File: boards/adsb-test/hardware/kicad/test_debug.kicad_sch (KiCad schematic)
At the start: 0 parts

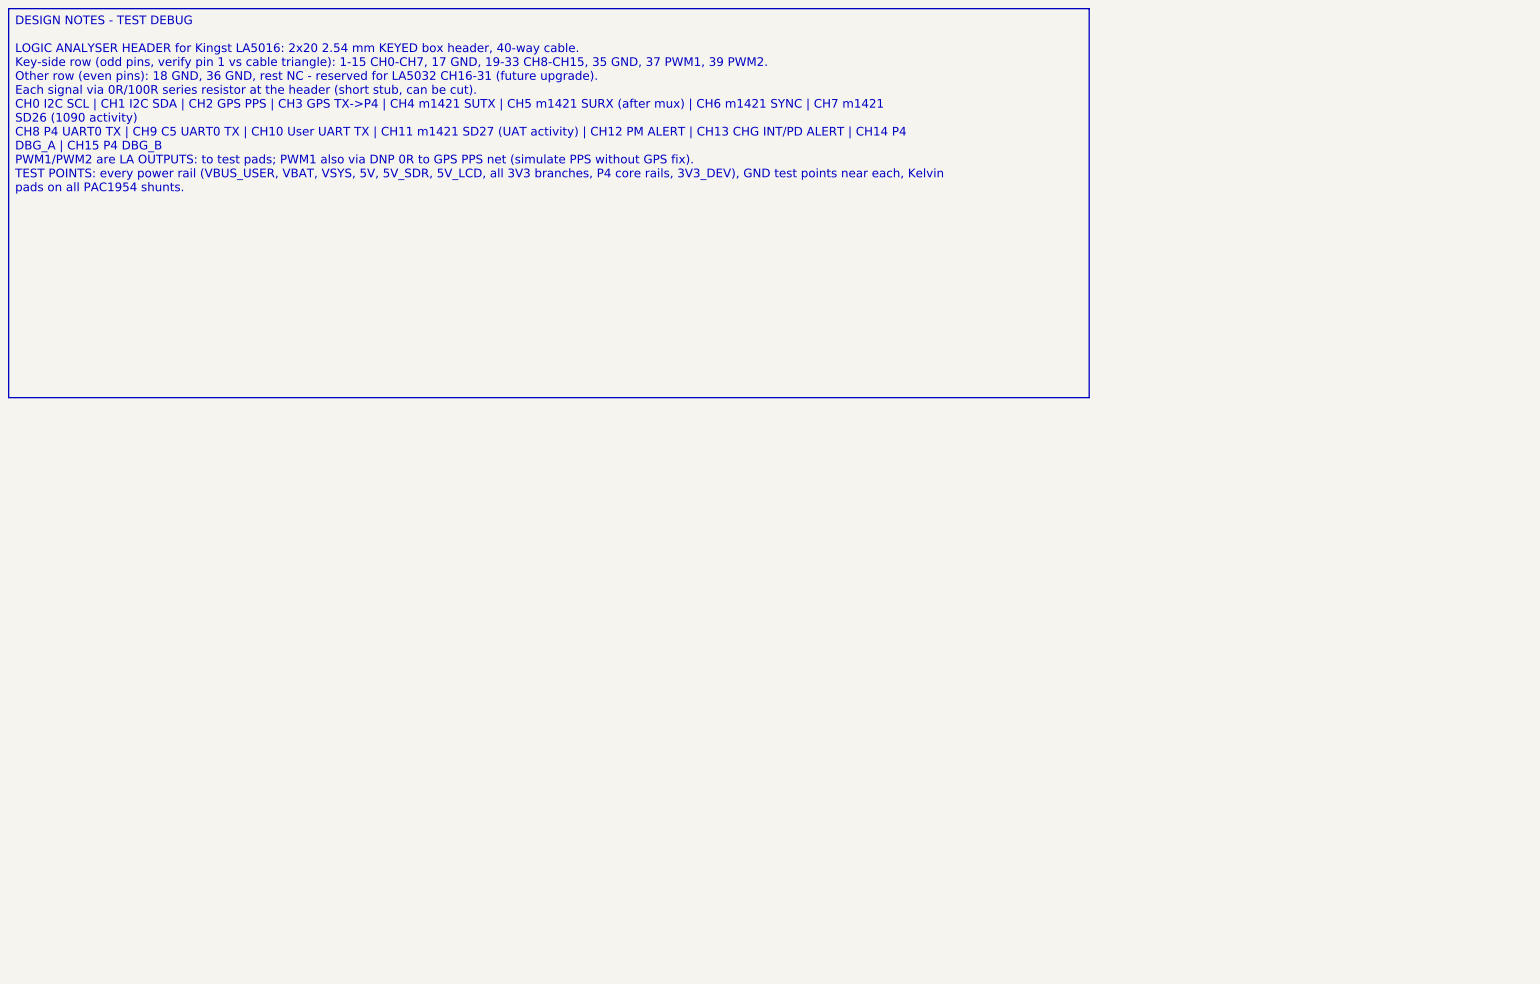
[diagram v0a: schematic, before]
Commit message: Release v0.22.0: all ADSB_Test schematic sheets generated (ERC clean)
Co-Authored-By: Claude Opus 5.5 <noreply@anthropic.com>
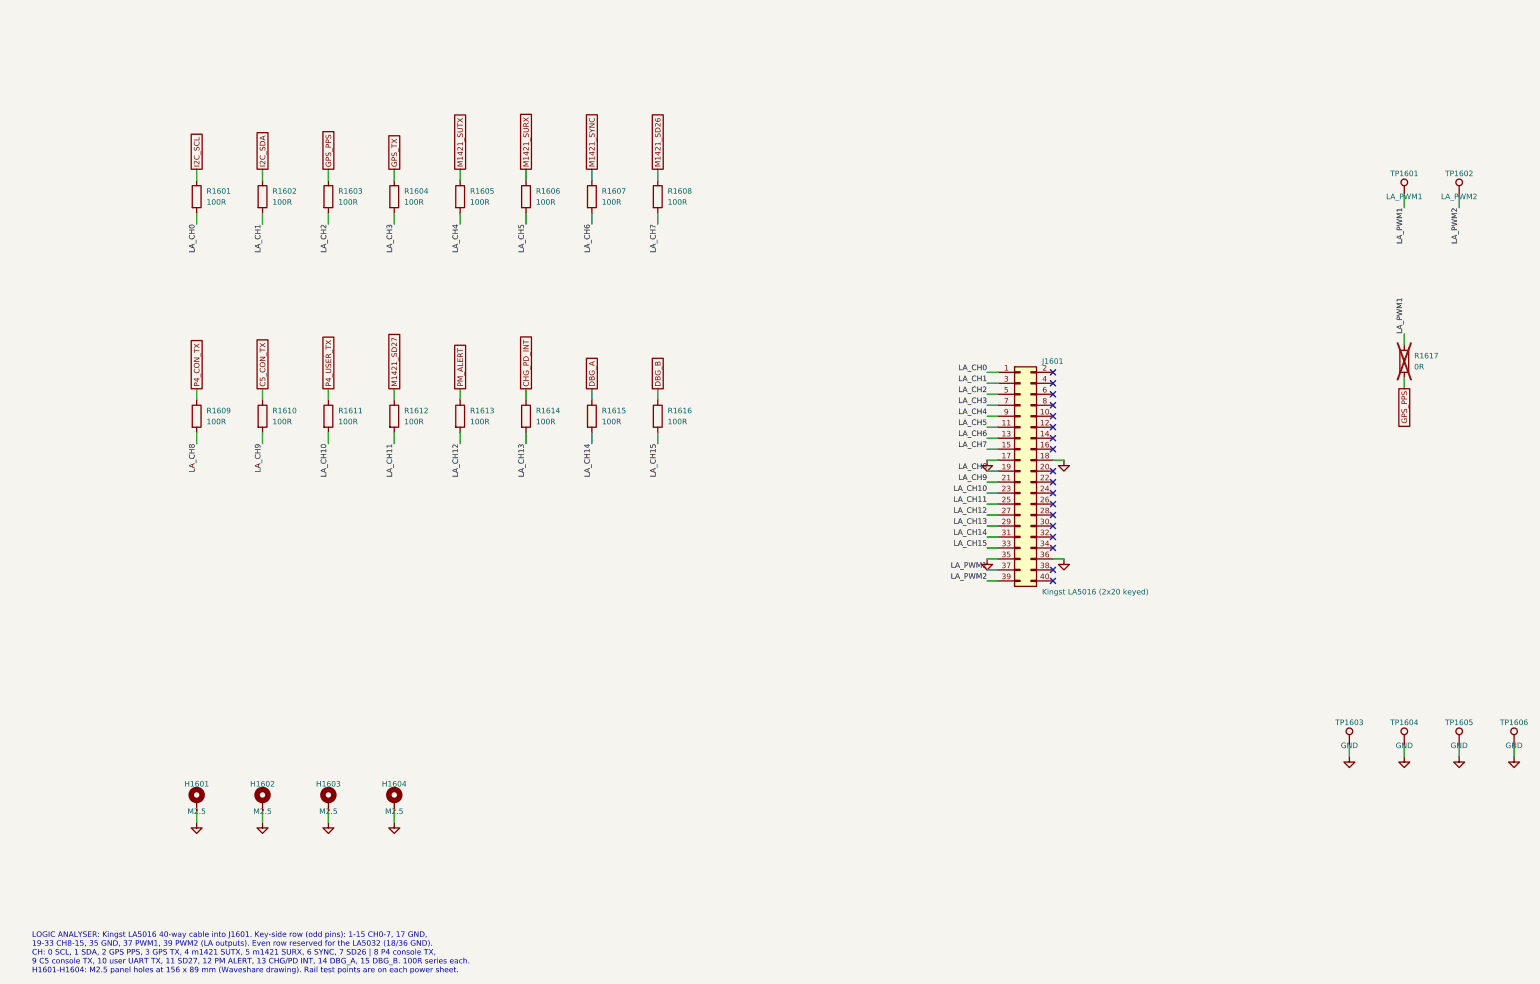
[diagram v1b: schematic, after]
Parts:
- added H1601, H1602, H1603, H1604: M2.5, MountingHole:MountingHole_2.7mm_M2.5_Pad_Via, symbol Mechanical:MountingHole_Pad
- added J1601: Kingst LA5016 (2x20 keyed), Connector_IDC:IDC-Header_2x20_P2.54mm_Vertical, symbol Connector_Generic:Conn_02x20_Odd_Even
- added R1601, R1602, R1603, R1604, R1605, R1606, R1607, R1608, R1609, R1610, R1611, R1612, R1613, R1614, R1615, R1616: 100R, Resistor_SMD:R_0805_2012Metric_Pad1.20x1.40mm_HandSolder, symbol Device:R
- added R1617: 0R, Resistor_SMD:R_0805_2012Metric_Pad1.20x1.40mm_HandSolder, symbol Device:R
- added TP1601: LA_PWM1, TestPoint:TestPoint_Pad_D1.5mm, symbol Connector:TestPoint
- added TP1602: LA_PWM2, TestPoint:TestPoint_Pad_D1.5mm, symbol Connector:TestPoint
- added TP1603, TP1604, TP1605, TP1606: GND, TestPoint:TestPoint_Pad_D1.5mm, symbol Connector:TestPoint
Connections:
- new net C5_CON_TX: R1610.1
- new net CHG_PD_INT: R1614.1
- new net DBG_A: R1615.1
- new net DBG_B: R1616.1
- new net GND: H1601.1, H1602.1, H1603.1, H1604.1, J1601.17 (Pin_17), J1601.18 (Pin_18), J1601.35 (Pin_35), J1601.36 (Pin_36), TP1603.1, TP1604.1, TP1605.1, TP1606.1
- new net GPS_PPS: R1603.1, R1617.2
- new net GPS_TX: R1604.1
- new net I2C_SCL: R1601.1
- new net I2C_SDA: R1602.1
- new net LA_CH0: J1601.1 (Pin_1), R1601.2
- new net LA_CH1: J1601.3 (Pin_3), R1602.2
- new net LA_CH10: J1601.23 (Pin_23), R1611.2
- new net LA_CH11: J1601.25 (Pin_25), R1612.2
- new net LA_CH12: J1601.27 (Pin_27), R1613.2
- new net LA_CH13: J1601.29 (Pin_29), R1614.2
- new net LA_CH14: J1601.31 (Pin_31), R1615.2
- new net LA_CH15: J1601.33 (Pin_33), R1616.2
- new net LA_CH2: J1601.5 (Pin_5), R1603.2
- new net LA_CH3: J1601.7 (Pin_7), R1604.2
- new net LA_CH4: J1601.9 (Pin_9), R1605.2
- new net LA_CH5: J1601.11 (Pin_11), R1606.2
- new net LA_CH6: J1601.13 (Pin_13), R1607.2
- new net LA_CH7: J1601.15 (Pin_15), R1608.2
- new net LA_CH8: J1601.19 (Pin_19), R1609.2
- new net LA_CH9: J1601.21 (Pin_21), R1610.2
- new net LA_PWM1: J1601.37 (Pin_37), R1617.1, TP1601.1
- new net LA_PWM2: J1601.39 (Pin_39), TP1602.1
- new net M1421_SD26: R1608.1
- new net M1421_SD27: R1612.1
- new net M1421_SURX: R1606.1
- new net M1421_SUTX: R1605.1
- new net M1421_SYNC: R1607.1
- new net P4_CON_TX: R1609.1
- new net P4_USER_TX: R1611.1
- new net PM_ALERT: R1613.1
- no-connect marks 0 -> 18
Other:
- note added: "LOGIC ANALYSER: Kingst LA5016 40-way cable into J1601. Key-side row (odd pins): 1-15 CH0-7, 17 GND, 19-33 CH8-15, 35 GND, 37 PWM1, 39 PWM2 (LA outputs). Even row reserved for the LA5032 (18/36 GND). CH: 0 SCL, 1 SDA, 2 GPS PPS, 3 GPS TX, 4 m1421 SUTX, 5 m1421 SURX, 6 SYNC, 7 SD26 | 8 P4 console TX, 9 C5 console TX, 10 user UART TX, 11 SD27, 12 PM ALERT, 13 CHG/PD INT, 14 DBG_A, 15 DBG_B. 100R ser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"
